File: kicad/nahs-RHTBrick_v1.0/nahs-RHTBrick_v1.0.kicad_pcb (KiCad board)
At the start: 2 copper layers, 45 x 70 mm, 68 parts, among them IC1 ESP12S, J2 USB_B_Mini, Q1 8205A, Q3 CJ2302, Q4 MMBT2907A, SW1 KMR_231_G_LFS, SW2 SSSS820101, U1 ZD8028IB5TR, U2 HDC1080, U3 DW01A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

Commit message: v1.0 Board - adjustments on bottom layer silkscreen
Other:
- board text added: "CHRG-ADJ"
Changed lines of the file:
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@@
   (gr_line (start 136.6 70) (end 100 70) (layer "Edge.Cuts") (width 0.1))
   (gr_circle (center 105 90) (end 107 90) (layer "Edge.Cuts") (width 0.1) (fill none))
+  (gr_text "CHRG-ADJ" (at 120.72 72.2) (layer "B.SilkS")
+    (effects (font (size 1.1 1.1) (thickness 0.16)) (justify mirror))
+  )
   (gr_text "S" (at 104.8 108.73) (layer "B.SilkS")
     (effects (font (size 1 1) (thickness 0.15)) (justify mirror))
@@
     (effects (font (size 1 1) (thickness 0.15)) (justify mirror))
   )
-  (gr_text "RXD" (at 133.2484 83.27) (layer "B.SilkS")
-    (effects (font (size 1 1) (thickness 0.15)) (justify right mirror))
+  (gr_text "RXD" (at 131.3516 83.27) (layer "B.SilkS")
+    (effects (font (size 1 1) (thickness 0.15)) (justify left mirror))
   )
   (gr_text "P" (at 104.8 111.27) (layer "B.SilkS")
@@
     (effects (font (size 1 1) (thickness 0.15)) (justify mirror))
   )
-  (gr_text "TXD" (at 133.2484 80.73) (layer "B.SilkS")
-    (effects (font (size 1 1) (thickness 0.15)) (justify right mirror))
+  (gr_text "TXD" (at 131.3516 80.73) (layer "B.SilkS")
+    (effects (font (size 1 1) (thickness 0.15)) (justify left mirror))
   )
   (gr_text "-" (at 104.8 100) (layer "B.SilkS")
     (effects (font (size 1 1) (thickness 0.15)) (justify mirror))
   )
-  (gr_text "GND" (at 133.2484 85.81) (layer "B.SilkS")
-    (effects (font (size 1 1) (thickness 0.15)) (justify right mirror))
+  (gr_text "GND" (at 131.3516 85.81) (layer "B.SilkS")
+    (effects (font (size 1 1) (thickness 0.15)) (justify left mirror))
   )
   (gr_text "+" (at 104.8 97.46) (layer "B.SilkS")
@@
     (effects (font (size 1 1) (thickness 0.15)) (justify mirror))
   )
-  (gr_text "5V" (at 133.2484 78.19) (layer "B.SilkS")
-    (effects (font (size 1 1) (thickness 0.15)) (justify right mirror))
+  (gr_text "5V" (at 131.3516 78.19) (layer "B.SilkS")
+    (effects (font (size 1 1) (thickness 0.15)) (justify left mirror))
   )
   (gr_text "by NiJO's" (at 125.7808 135.9408) (layer "B.SilkS")
@@
   (segment (start 129.413 107.315) (end 129.794 106.934) (width 0.254) (layer "B.Cu") (net 40))
   (segment (start 127.777 107.315) (end 129.413 107.315) (width 0.254) (layer "B.Cu") (net 40))
+  (segment (start 132.588 79.502) (end 134.366 77.724) (width 0.254) (layer "F.Cu") (net 41))
   (segment (start 131.85019 79.502) (end 132.588 79.502) (width 0.254) (layer "F.Cu") (net 41))
+  (segment (start 128.778 86.868) (end 128.718 86.928) (width 0.254) (layer "F.Cu") (net 41))
+  (segment (start 129.032011 82.117595) (end 129.234595 82.117595) (width 0.254) (layer "F.Cu") (net 41))
   (segment (start 127.635 86.128) (end 127.635 86.928) (width 0.254) (layer "F.Cu") (net 41))
-  (segment (start 132.588 79.502) (end 134.366 77.724) (width 0.254) (layer "F.Cu") (net 41))
-  (segment (start 134.366 77.724) (end 134.366 76.962) (width 0.254) (layer "F.Cu") (net 41))
-  (segment (start 129.032 82.55) (end 129.032 82.32019) (width 0.254) (layer "F.Cu") (net 41))
-  (segment (start 128.21 86.928) (end 128.778 86.36) (width 0.254) (layer "F.Cu") (net 41))
-  (segment (start 129.032 82.32019) (end 131.85019 79.502) (width 0.254) (layer "F.Cu") (net 41))
+  (segment (start 128.718 86.928) (end 127.635 86.928) (width 0.254) (layer "F.Cu") (net 41))
+  (segment (start 129.234595 82.117595) (end 131.85019 79.502) (width 0.254) (layer "F.Cu") (net 41))
   (segment (start 126.911511 85.404511) (end 127.635 86.128) (width 0.254) (layer "F.Cu") (net 41))
   (segment (start 122.174 82.9545) (end 122.174 83.525022) (width 0.254) (layer "F.Cu") (net 41))
-  (segment (start 127.635 86.928) (end 128.21 86.928) (width 0.254) (layer "F.Cu") (net 41))
+  (segment (start 134.366 77.724) (end 134.366 76.962) (width 0.254) (layer "F.Cu") (net 41))
   (segment (start 124.053489 85.404511) (end 126.911511 85.404511) (width 0.254) (layer "F.Cu") (net 41))
   (segment (start 122.174 83.525022) (end 124.053489 85.404511) (width 0.254) (layer "F.Cu") (net 41))
   (via (at 134.366 76.962) (size 0.8) (drill 0.4) (layers "F.Cu" "B.Cu") (net 41))
-  (via (at 129.032 82.55) (size 0.8) (drill 0.4) (layers "F.Cu" "B.Cu") (net 41))
-  (via (at 128.778 86.36) (size 0.8) (drill 0.4) (layers "F.Cu" "B.Cu") (net 41))
+  (via (at 129.032011 82.117595) (size 0.8) (drill 0.4) (layers "F.Cu" "B.Cu") (net 41))
+  (via (at 128.778 86.868) (size 0.8) (drill 0.4) (layers "F.Cu" "B.Cu") (net 41))
+  (segment (start 126.467216 79.5528) (end 129.032011 82.117595) (width 0.254) (layer "B.Cu") (net 41))
+  (segment (start 129.032 82.117606) (end 129.032011 82.117595) (width 0.254) (layer "B.Cu") (net 41))
   (segment (start 136.678 74.65) (end 141.55 74.65) (width 0.254) (layer "B.Cu") (net 41))
-  (segment (start 128.778 86.36) (end 129.032 86.106) (width 0.254) (layer "B.Cu") (net 41))
+  (segment (start 122.0724 79.5528) (end 126.467216 79.5528) (width 0.254) (layer "B.Cu") (net 41))
   (segment (start 117.094 84.5312) (end 122.0724 79.5528) (width 0.254) (layer "B.Cu") (net 41))
-  (segment (start 122.0724 79.5528) (end 126.0348 79.5528) (width 0.254) (layer "B.Cu") (net 41))
   (segment (start 134.366 76.962) (end 136.678 74.65) (width 0.254) (layer "B.Cu") (net 41))
-  (segment (start 129.032 86.106) (end 129.032 82.55) (width 0.254) (layer "B.Cu") (net 41))
-  (segment (start 126.0348 79.5528) (end 129.032 82.55) (width 0.254) (layer "B.Cu") (net 41))
+  (segment (start 128.778 86.868) (end 129.032 86.614) (width 0.254) (layer "B.Cu") (net 41))
+  (segment (start 129.032 86.614) (end 129.032 82.117606) (width 0.254) (layer "B.Cu") (net 41))
   (segment (start 130.572 71.45) (end 132.572 71.45) (width 0.254) (layer "F.Cu") (net 45))
   (segment (start 135.072 71.45) (end 134.472 71.45) (width 0.254) (layer "F.Cu") (net 45))

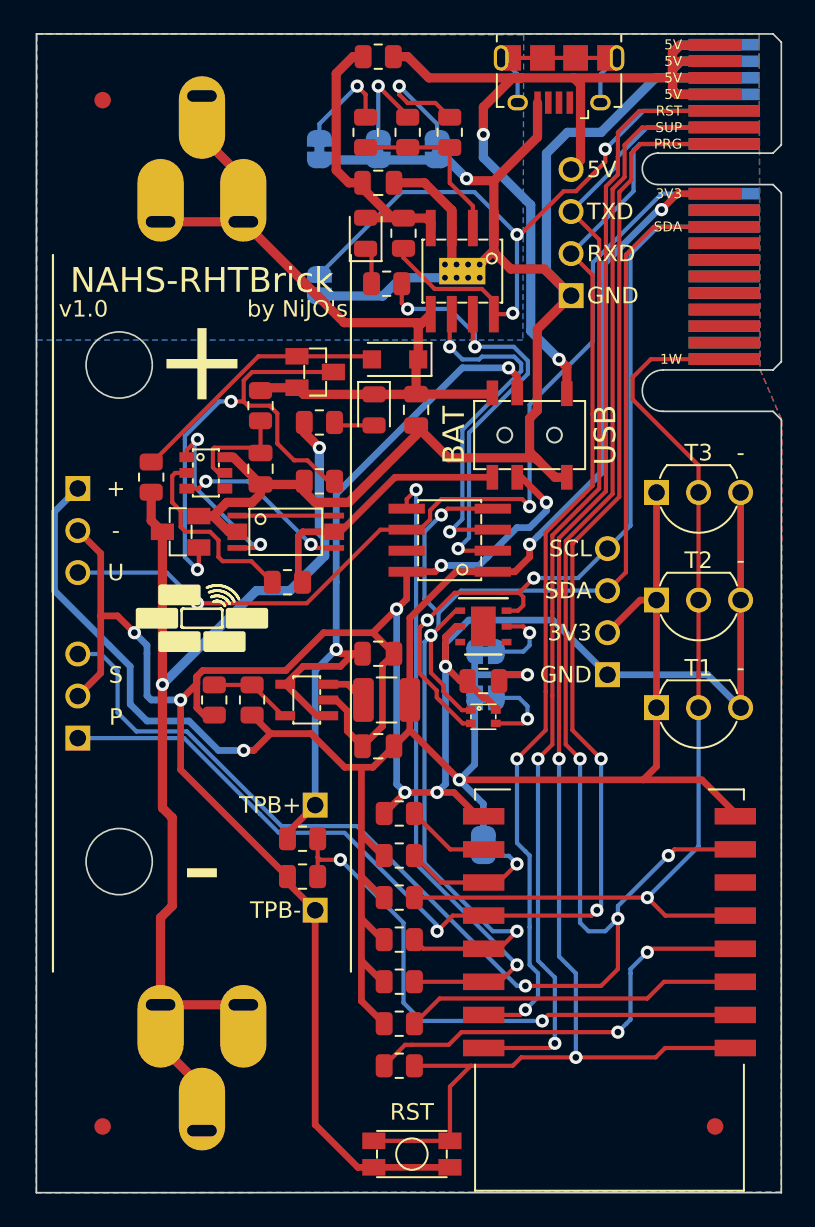
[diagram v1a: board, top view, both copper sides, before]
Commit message: v1.0 Board done; v1.0 Breakout Board done
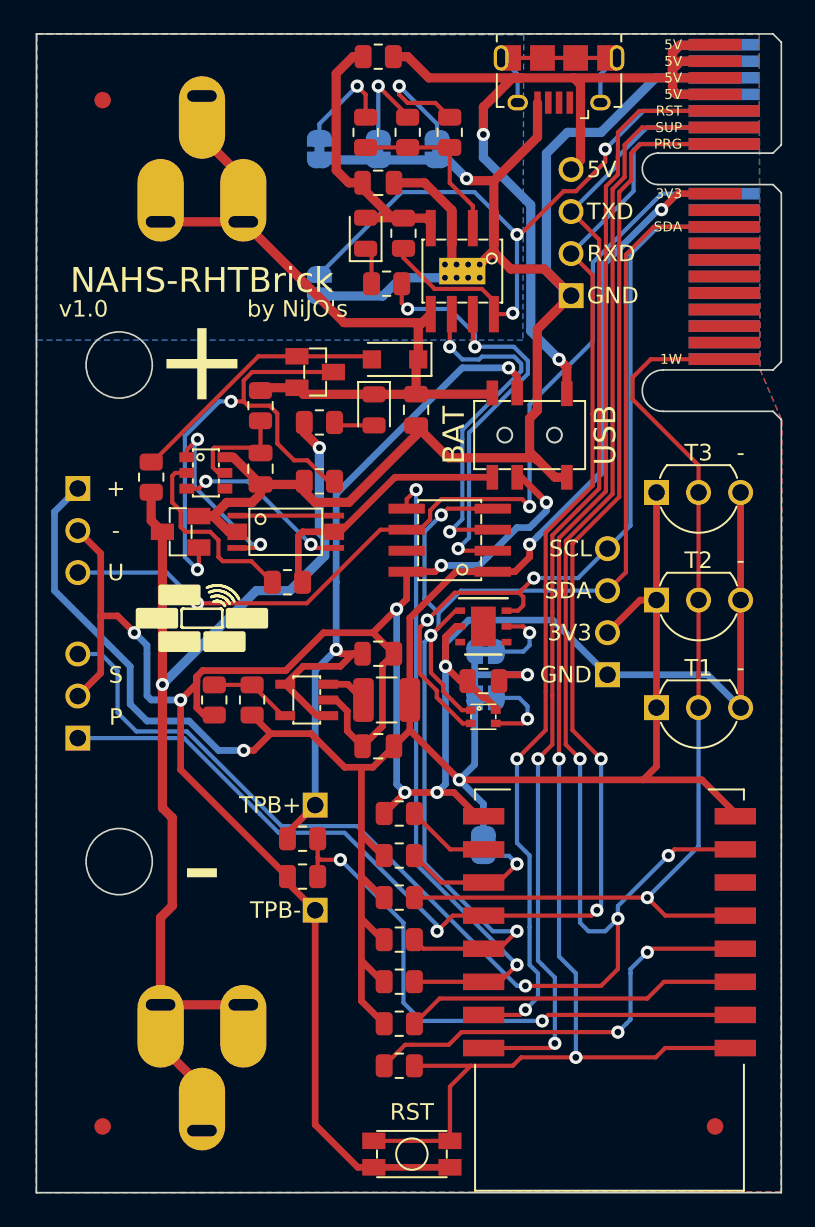
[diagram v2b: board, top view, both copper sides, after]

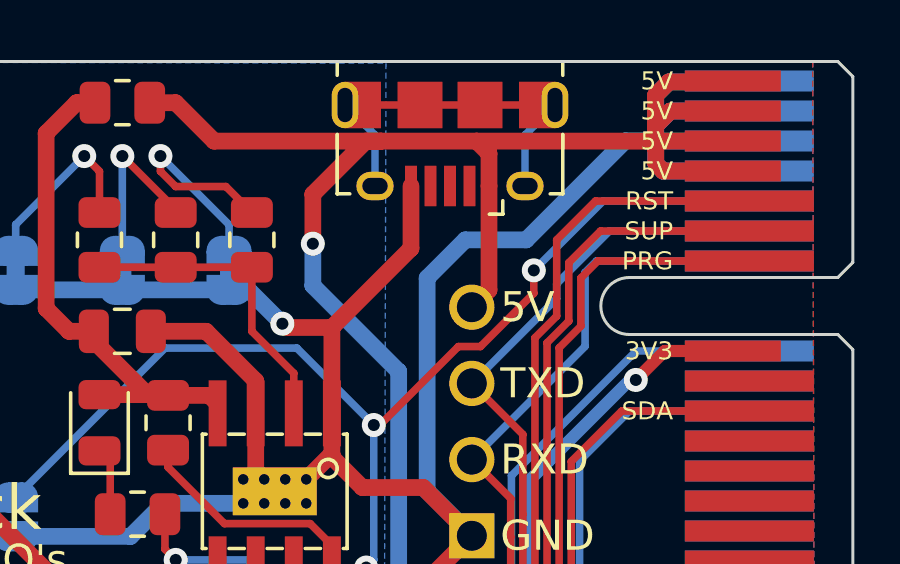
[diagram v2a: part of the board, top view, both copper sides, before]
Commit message: updated footprints for stencil
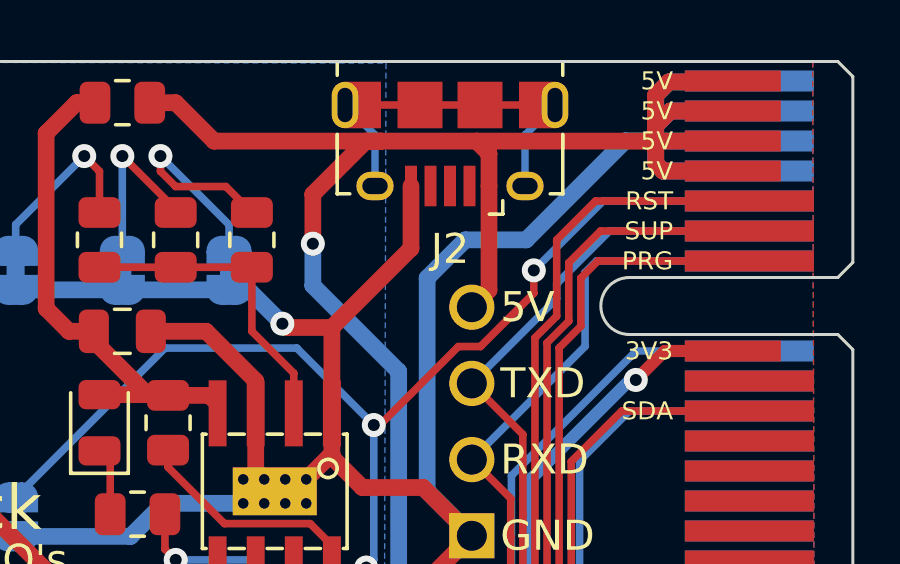
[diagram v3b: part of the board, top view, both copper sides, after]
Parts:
- J2: footprint Connector_USB:USB_Micro-B_Amphenol_10118194_Horizontal -> no_common:USB_Micro-B_Amphenol_10118194_Horizontal
